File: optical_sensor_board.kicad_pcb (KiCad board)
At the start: 2 copper layers, 73 x 45.5 mm, 42 parts, among them J2 Conn_01x09_Socket, U1 PMW3389DM‐T3QU, U3 LM317L_SOT-89

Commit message: Added a solder-jumer in series to the PS of the chip
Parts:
- added JP101: SolderJumper_2_Open, Jumper:SolderJumper-2_P1.3mm_Open_TrianglePad1.0x1.5mm, B.Cu at (156.2, 60.7)
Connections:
- U1 pad 4: VDD -> Net-(JP101-B)
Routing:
- net VDD: track 231.0 -> 211.5 mm
- net Net-(JP101-B): track 0.00 -> 17.1 mm
- net GND: track 241.9 -> 243.5 mm
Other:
- board text added: "Rev 1.1"
- board text added: "pmw3389-board Rev 1.1"
- board text removed: "RV1"
- board text removed: "pmw3389-board RV1"

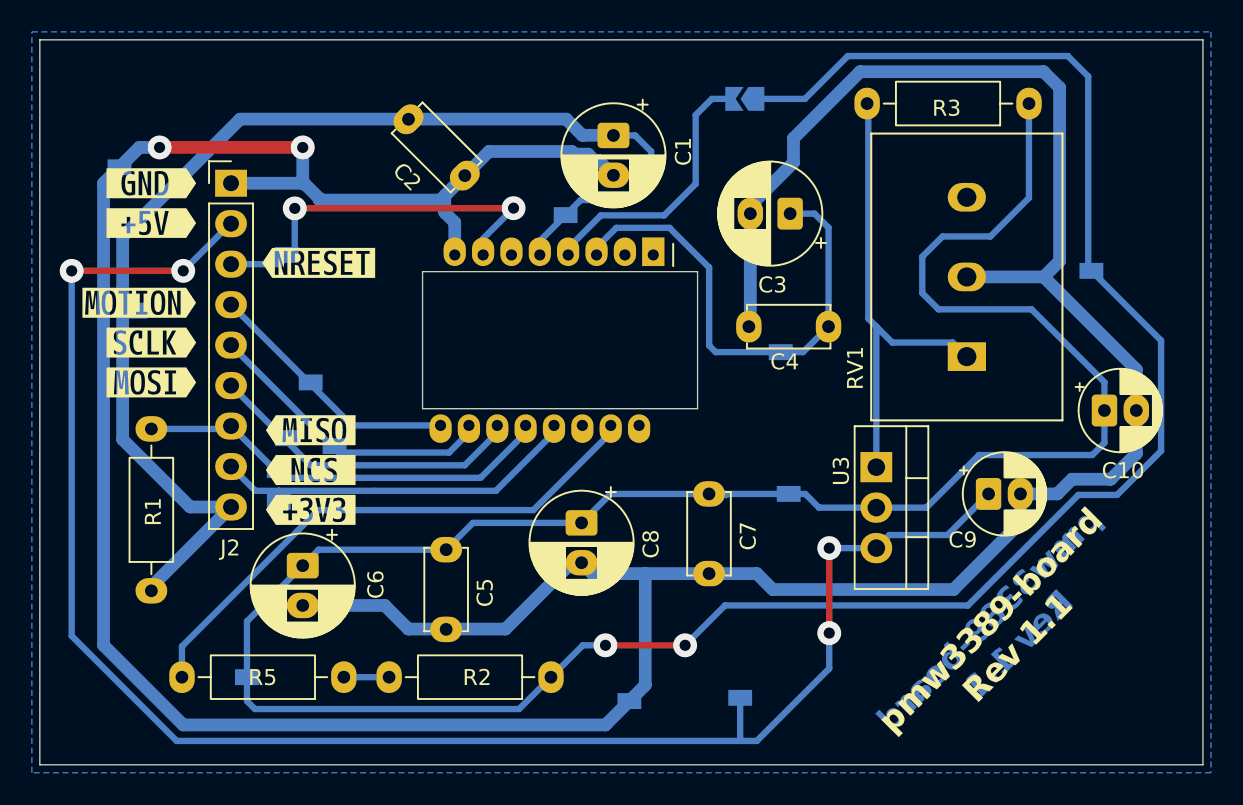
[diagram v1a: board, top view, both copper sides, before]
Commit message: Modified some traks of the PCB + exported new PDF for mastering
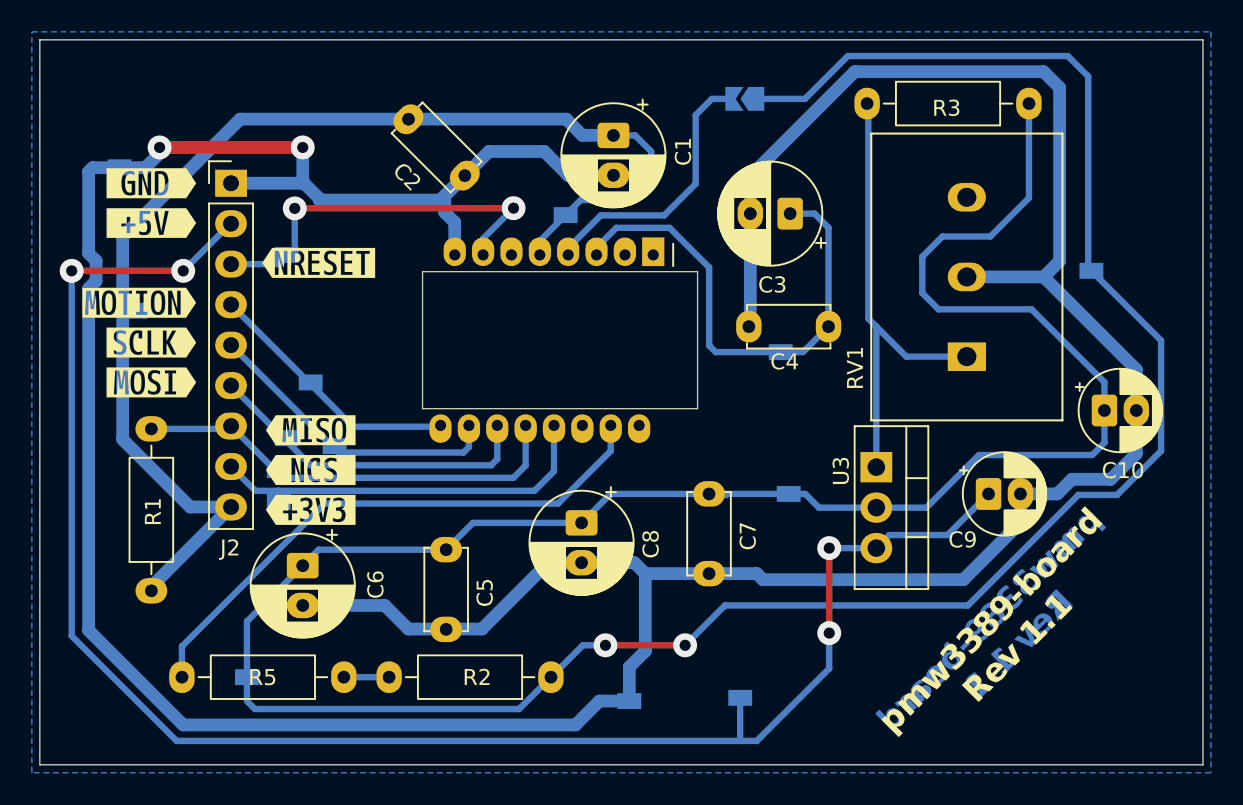
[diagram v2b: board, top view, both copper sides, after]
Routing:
- net GND: track 243.5 -> 245.6 mm
- net NCS: track 23.6 -> 25.0 mm
- net MISO: track 26.8 -> 28.0 mm
- net MOSI: track 20.2 -> 21.2 mm
- net LED_P: track 34.9 -> 35.5 mm
- net SCLK: track 18.7 -> 19.2 mm
